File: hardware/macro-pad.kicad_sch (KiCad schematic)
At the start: 22 parts

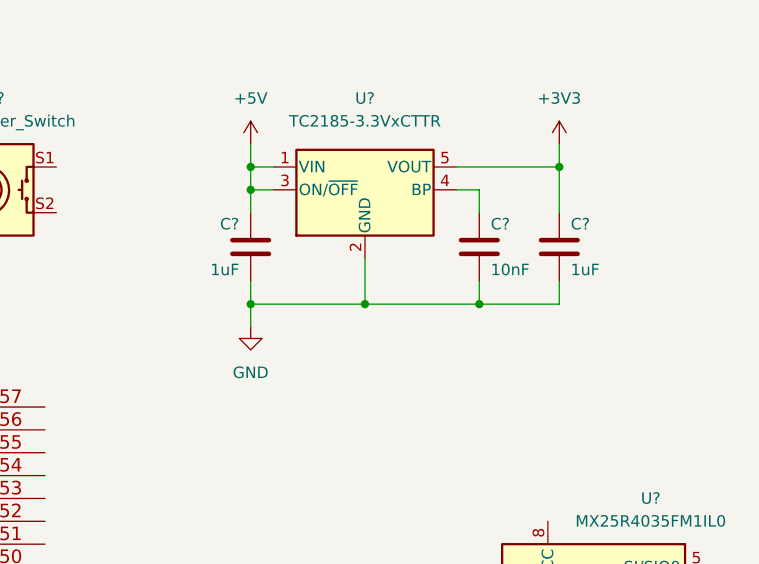
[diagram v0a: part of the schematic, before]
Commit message: Linear-reg was subsituted with a MIC5317
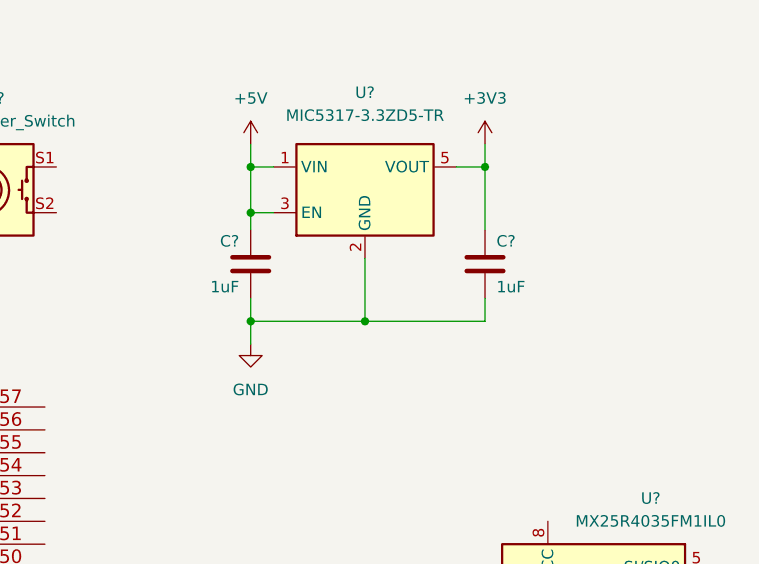
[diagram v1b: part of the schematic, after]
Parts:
- removed C?: 10nF, symbol Device:C
- removed U?: TC2185-3.3VxCTTR, Package_TO_SOT_SMD:SOT-23-5, symbol Regulator_Linear:TC2185-3.3VxCTTR
- added U?: MIC5317-3.3ZD5-TR, Package_TO_SOT_SMD:SOT-23-5, symbol Regulator_Linear:MIC5365-3.3YD5
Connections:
- net +3V3: now also U?.5 (VOUT)
- net +5V: now also U?.1 (VIN), U?.3 (EN)
- net GND: now also U?.2 (GND)
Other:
- moved on the sheet: C?

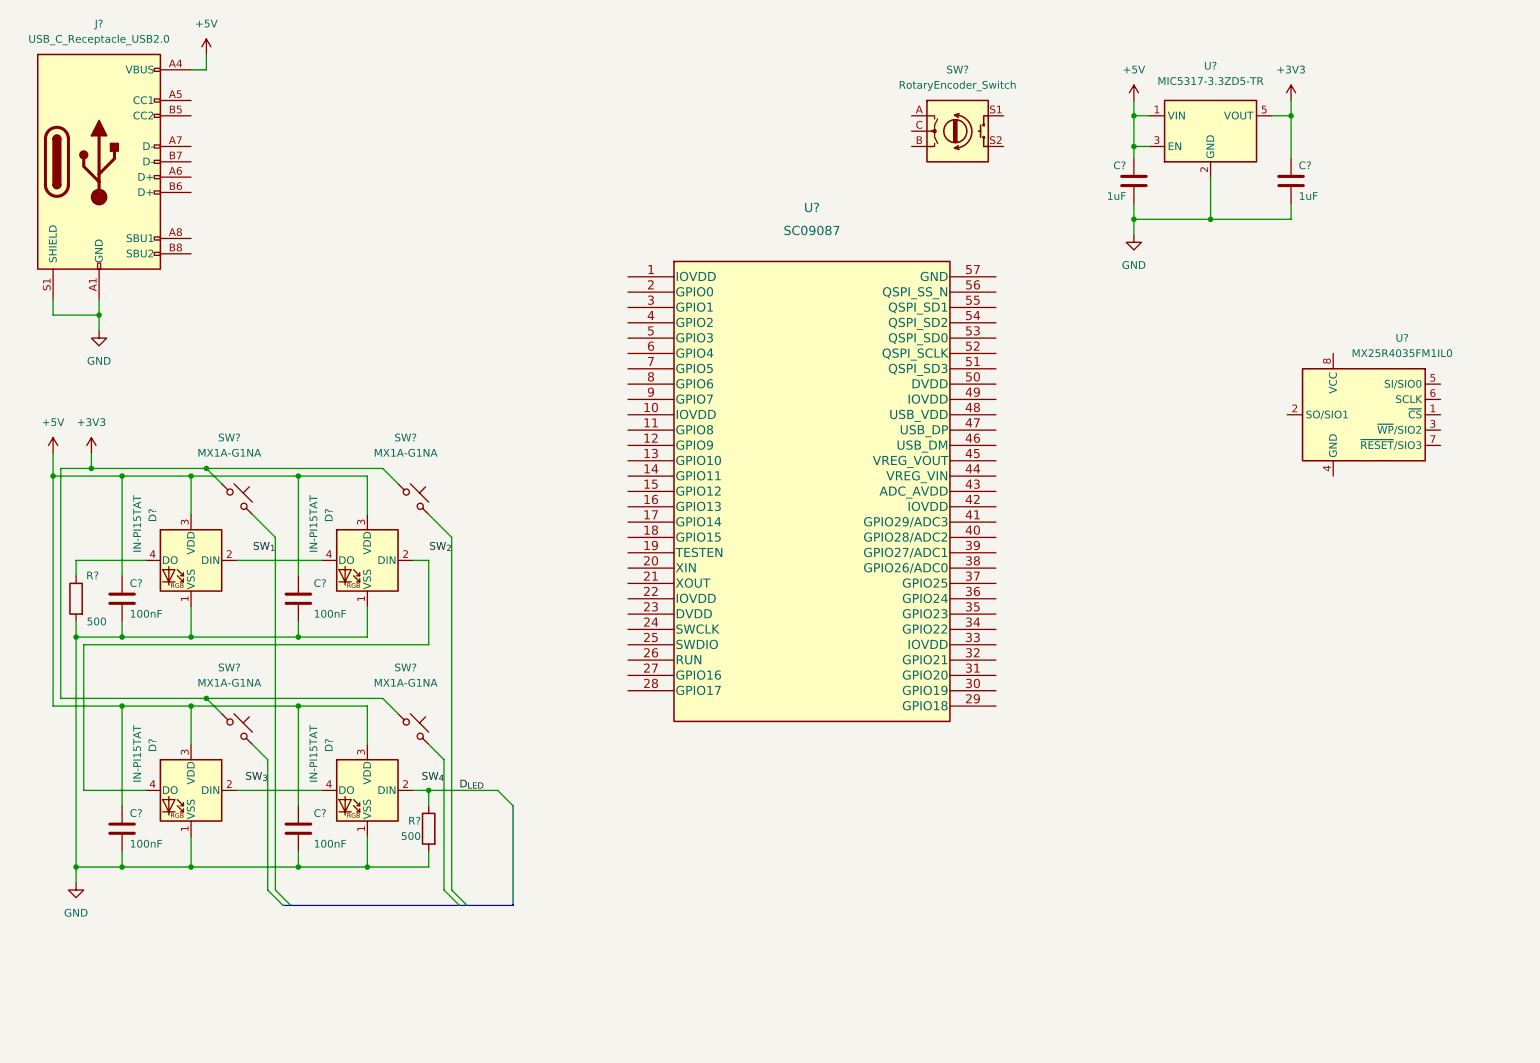
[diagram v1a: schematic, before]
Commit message: Added microcontroller symbol, power and USB data
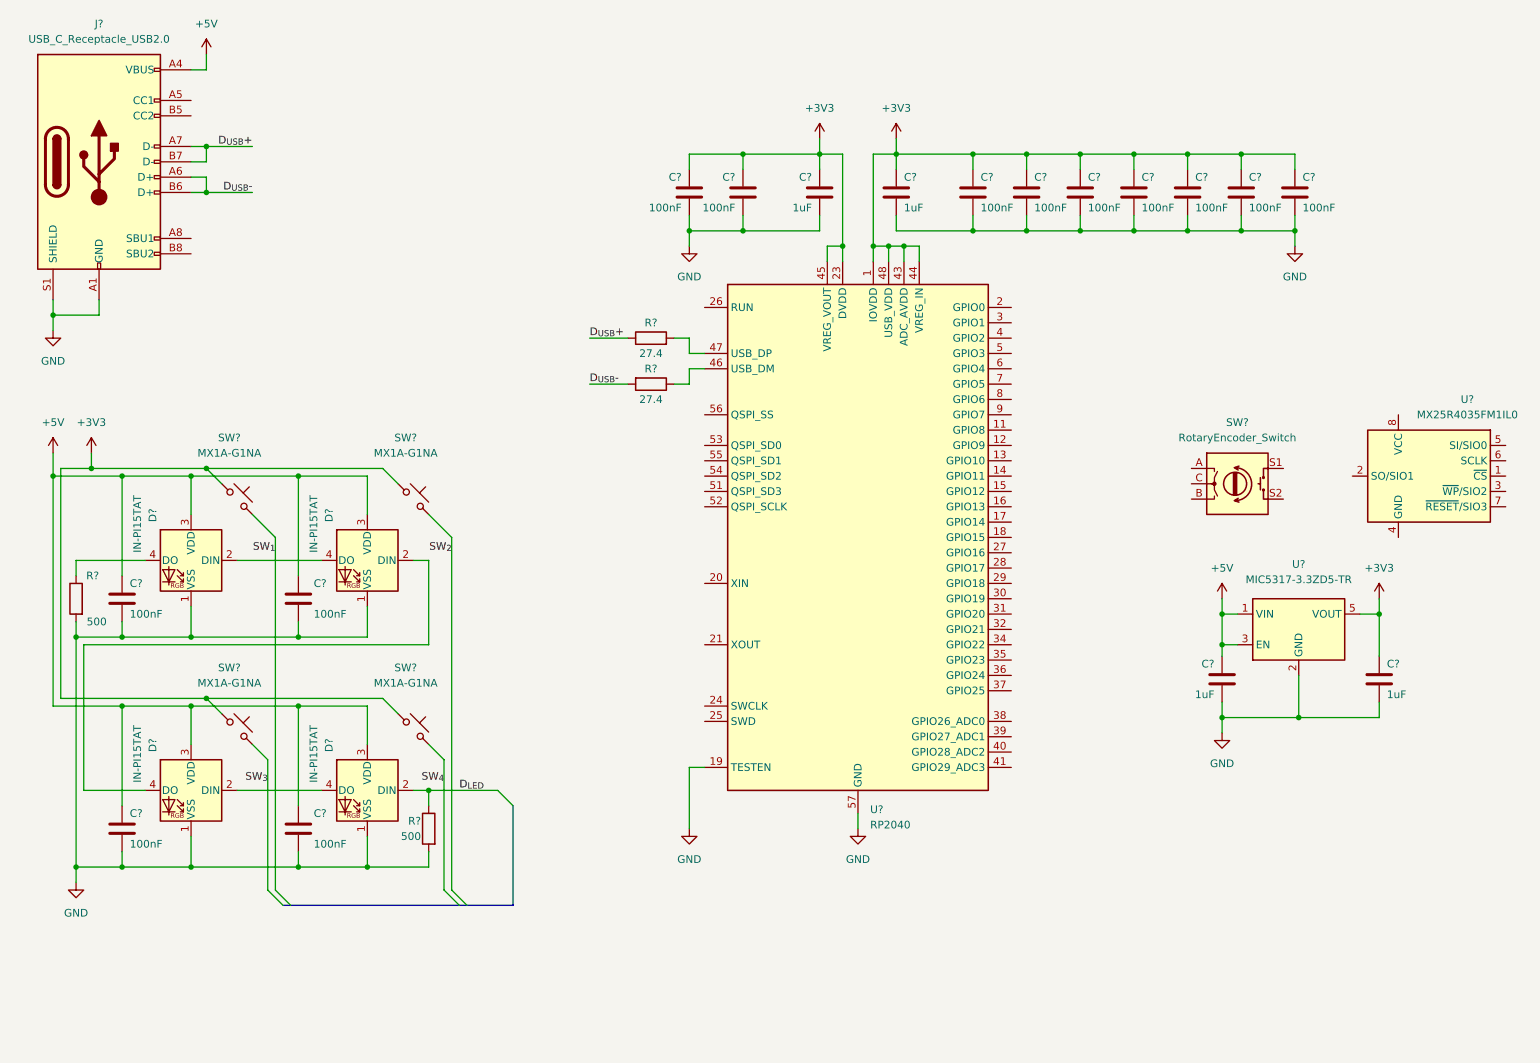
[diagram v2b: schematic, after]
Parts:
- removed U?: SC09087, IC57_RP2040, symbol SC09087:SC09087
- added C? (x9): 100nF, symbol Device:C
- added C? (x2): 1uF, symbol Device:C
- added R? (x2): 27.4, symbol Device:R
- added U?: RP2040, Package_DFN_QFN:QFN-56-1EP_7x7mm_P0.4mm_EP3.2x3.2mm, symbol MCU_RaspberryPi:RP2040
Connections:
- net +3V3: now also C?.1, C?.1, C?.1, C?.1, C?.1, C?.1, C?.1, C?.1, C?.1, C?.1, C?.1, U?.1 (IOVDD), U?.10 (IOVDD), U?.22 (IOVDD), U?.23 (DVDD), U?.33 (IOVDD), U?.42 (IOVDD), U?.43 (ADC_AVDD), U?.44 (VREG_IN), U?.45 (VREG_VOUT), U?.48 (USB_VDD), U?.49 (IOVDD), U?.50 (DVDD)
- net GND: now also C?.2, C?.2, C?.2, C?.2, C?.2, C?.2, C?.2, C?.2, C?.2, C?.2, C?.2, U?.19 (TESTEN), U?.57 (GND)
- net D_{USB}-: now reaches J?.A6 (D+)
- net D_{USB}-: now also J?.B6 (D+), R?.2
- net D_{USB}+: now reaches J?.A7 (D-)
- net D_{USB}+: now also J?.B7 (D-), R?.1
- new net: R?.2, U?.47 (USB_DP)
- new net: R?.1, U?.46 (USB_DM)
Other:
- moved on the sheet: C?, SW?, U?

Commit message: Added quarz crystal and wired up flash memory
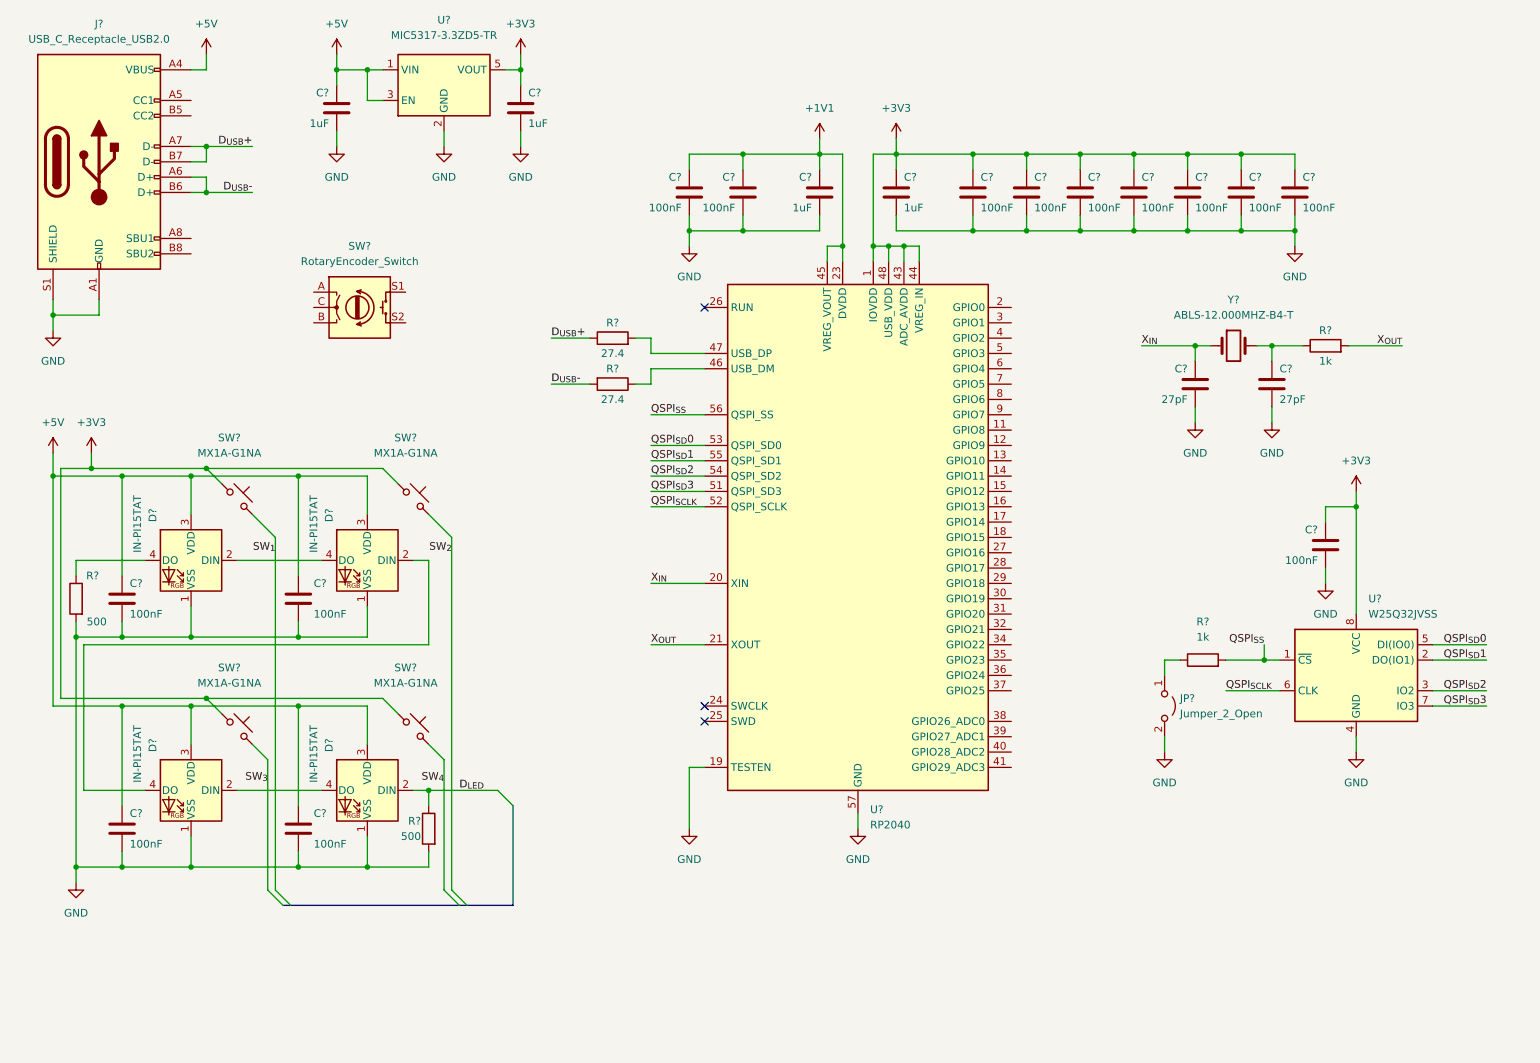
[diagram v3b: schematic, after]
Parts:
- removed U?: MX25R4035FM1IL0, Package_SO:SOP-8_3.9x4.9mm_P1.27mm, symbol Memory_Flash:MX25R3235FM1xx0
- added C? (x2): 27pF, symbol Device:C
- added C?: 100nF, symbol Device:C
- added JP?: Jumper_2_Open, symbol Jumper:Jumper_2_Open
- added R? (x2): 1k, symbol Device:R
- added U?: W25Q32JVSS, Package_SO:SOIC-8_5.23x5.23mm_P1.27mm, symbol Memory_Flash:W25Q32JVSS
- added Y?: ABLS-12.000MHZ-B4-T, symbol Device:Crystal
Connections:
- net +3V3: now also C?.1, U?.8 (VCC); no longer C?.1, C?.1, C?.1, U?.23 (DVDD), U?.45 (VREG_VOUT), U?.50 (DVDD)
- net GND: now also C?.2, C?.2, C?.2, JP?.2 (B), U?.4 (GND)
- net X_{IN}: now reaches U?.20 (XIN)
- net X_{IN}: now also C?.1, Y?.1
- net X_{OUT}: now reaches U?.21 (XOUT)
- net X_{OUT}: now also R?.2
- net QSPI_{SD}3: now reaches U?.51 (QSPI_SD3)
- net QSPI_{SD}3: now also U?.7 (IO3)
- net QSPI_{SCLK}: now reaches U?.52 (QSPI_SCLK)
- net QSPI_{SCLK}: now also U?.6 (CLK)
- net QSPI_{SD}0: now reaches U?.53 (QSPI_SD0)
- net QSPI_{SD}0: now also U?.5 (DI(IO0))
- net QSPI_{SD}2: now reaches U?.54 (QSPI_SD2)
- net QSPI_{SD}2: now also U?.3 (IO2)
- net QSPI_{SD}1: now reaches U?.55 (QSPI_SD1)
- net QSPI_{SD}1: now also U?.2 (DO(IO1))
- net QSPI_{SS}: now reaches U?.56 (QSPI_SS)
- net QSPI_{SS}: now also R?.2, U?.1 (~{CS})
- new net: JP?.1 (A), R?.1
- new net: C?.1, R?.1, Y?.2
- new net +1V1: C?.1, C?.1, C?.1, U?.23 (DVDD), U?.45 (VREG_VOUT), U?.50 (DVDD)
- no-connect marks 0 -> 3
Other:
- moved on the sheet: C?, R?, SW?, U?

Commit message: Added rotary encoder circuit
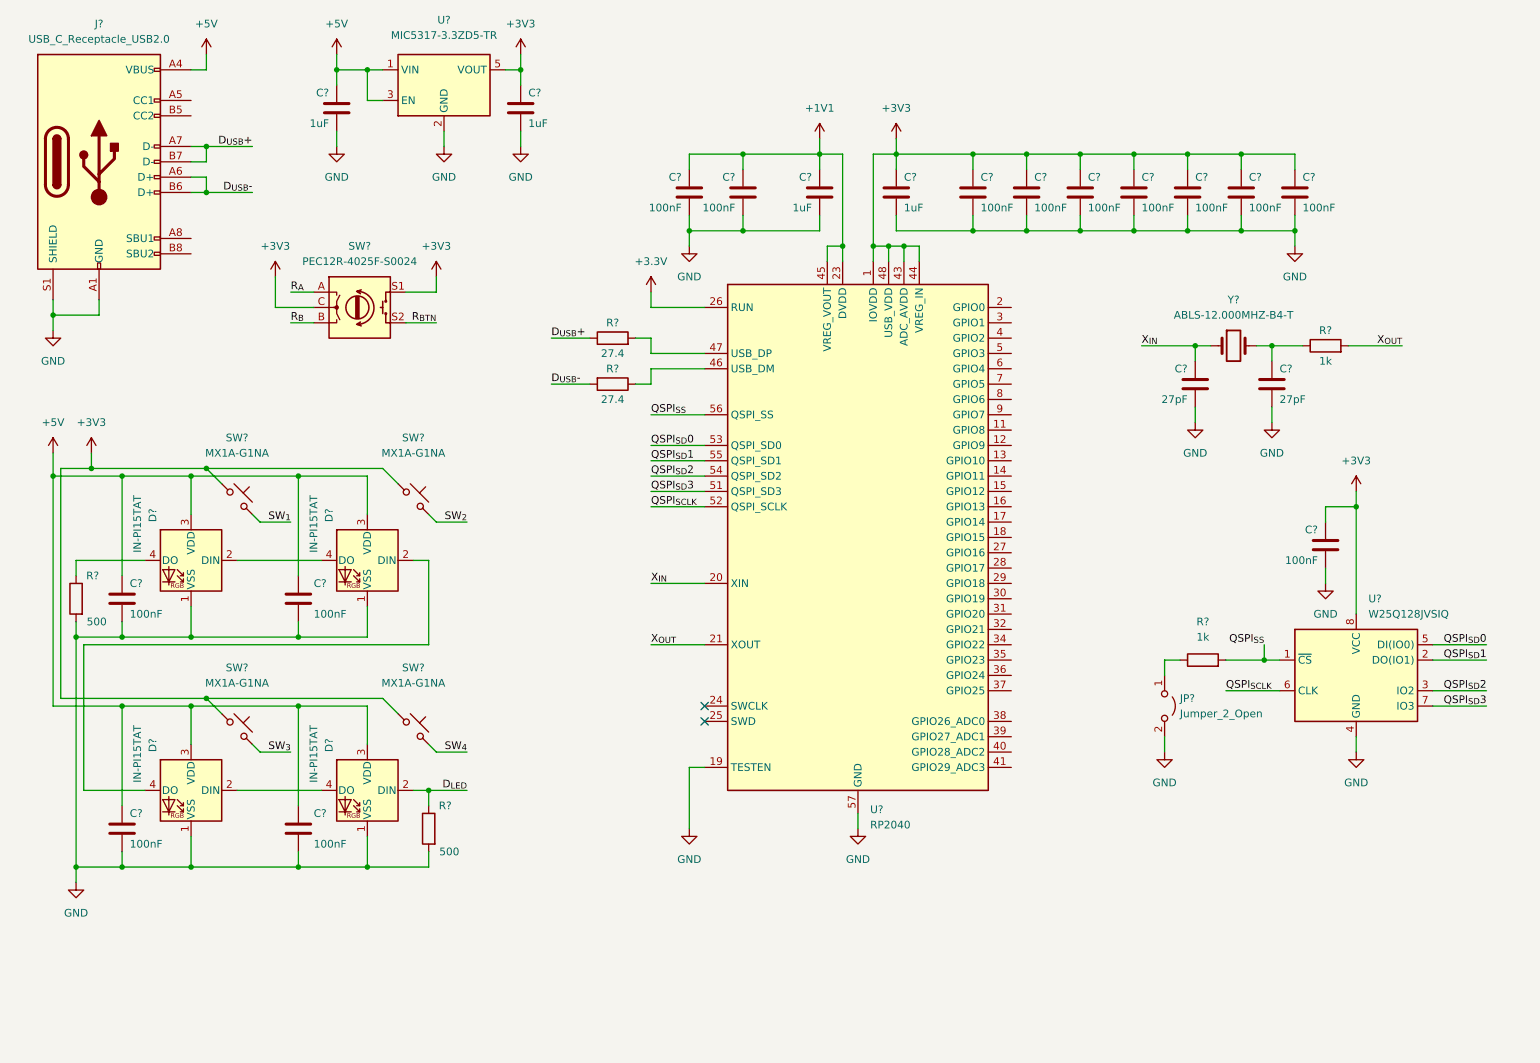
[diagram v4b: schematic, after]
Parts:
- removed R?: 500, symbol Device:R
- added R?: 500, symbol Device:R
- SW?: value RotaryEncoder_Switch -> PEC12R-4025F-S0024
- U?: value W25Q32JVSS -> W25Q128JVSIQ
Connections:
- net +3V3: now also SW?.C, SW?.S1
- net D_{LED}: now also R?.1
- net GND: now also R?.2
- net R_{A}: now reaches SW?.A
- net R_{B}: now reaches SW?.B
- net R_{BTN}: now reaches SW?.S2
- net +3.3V: now reaches U?.26 (RUN)
- no-connect marks 3 -> 2

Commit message: Box drawing, labelling and rearranging of components
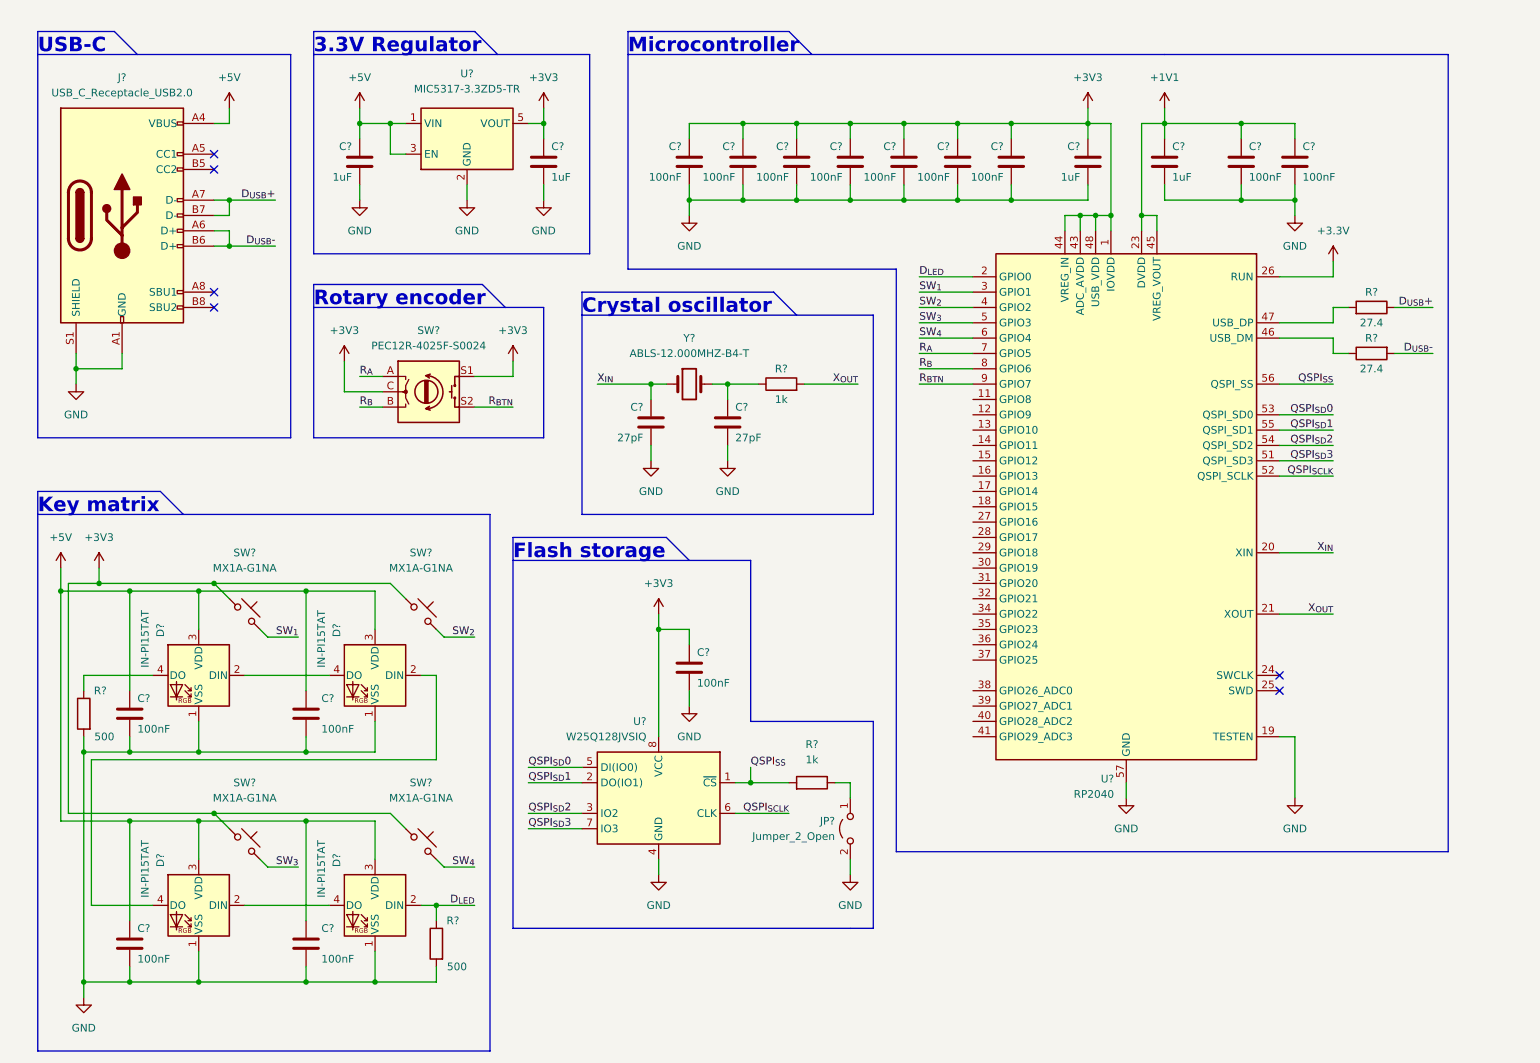
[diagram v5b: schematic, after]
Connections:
- net D_{LED}: now also U?.2 (GPIO0)
- net R_{A}: now also U?.7 (GPIO5)
- net R_{BTN}: now also U?.9 (GPIO7)
- net R_{B}: now also U?.8 (GPIO6)
- net SW_{1}: now also U?.3 (GPIO1)
- net SW_{2}: now also U?.4 (GPIO2)
- net SW_{3}: now also U?.5 (GPIO3)
- net SW_{4}: now also U?.6 (GPIO4)
- no-connect marks 2 -> 6
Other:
- note added: "3.3V Regulator"
- note added: "Crystal oscillator"
- note added: "Flash storage"
- note added: "Key matrix"
- note added: "Microcontroller"
- note added: "Rotary encoder"
- note added: "USB-C"
- moved on the sheet: C?, D?, J?, JP?, R?, SW?, U?, Y?
